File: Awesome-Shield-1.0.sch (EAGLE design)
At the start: 21 parts, among them J1 PORT1, J2 PORT2, J3 PORT3, SW1 SPST_TACT-EVQQ2, SW2 DPDT, U1 LIGHTSENSORTEMT6000, X1 PASSER-07, X2 PASSER-07

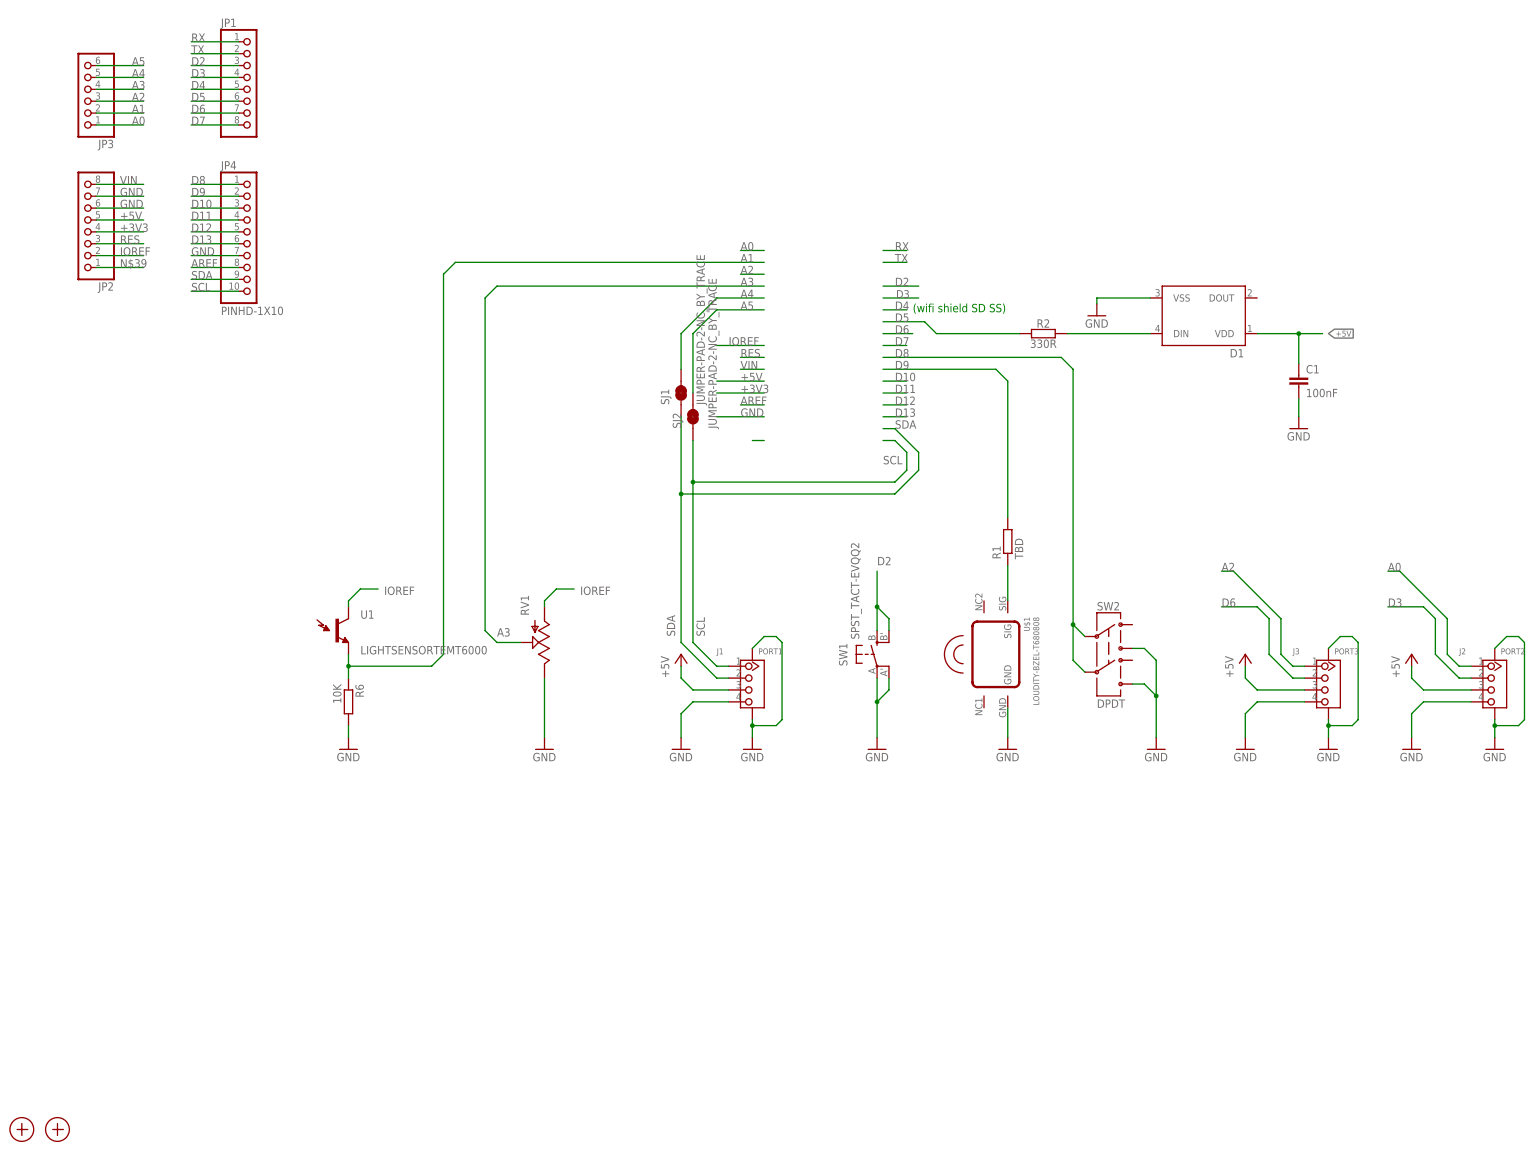
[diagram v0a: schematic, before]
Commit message: add resistors to button, toggleSwitch, knob signal lines
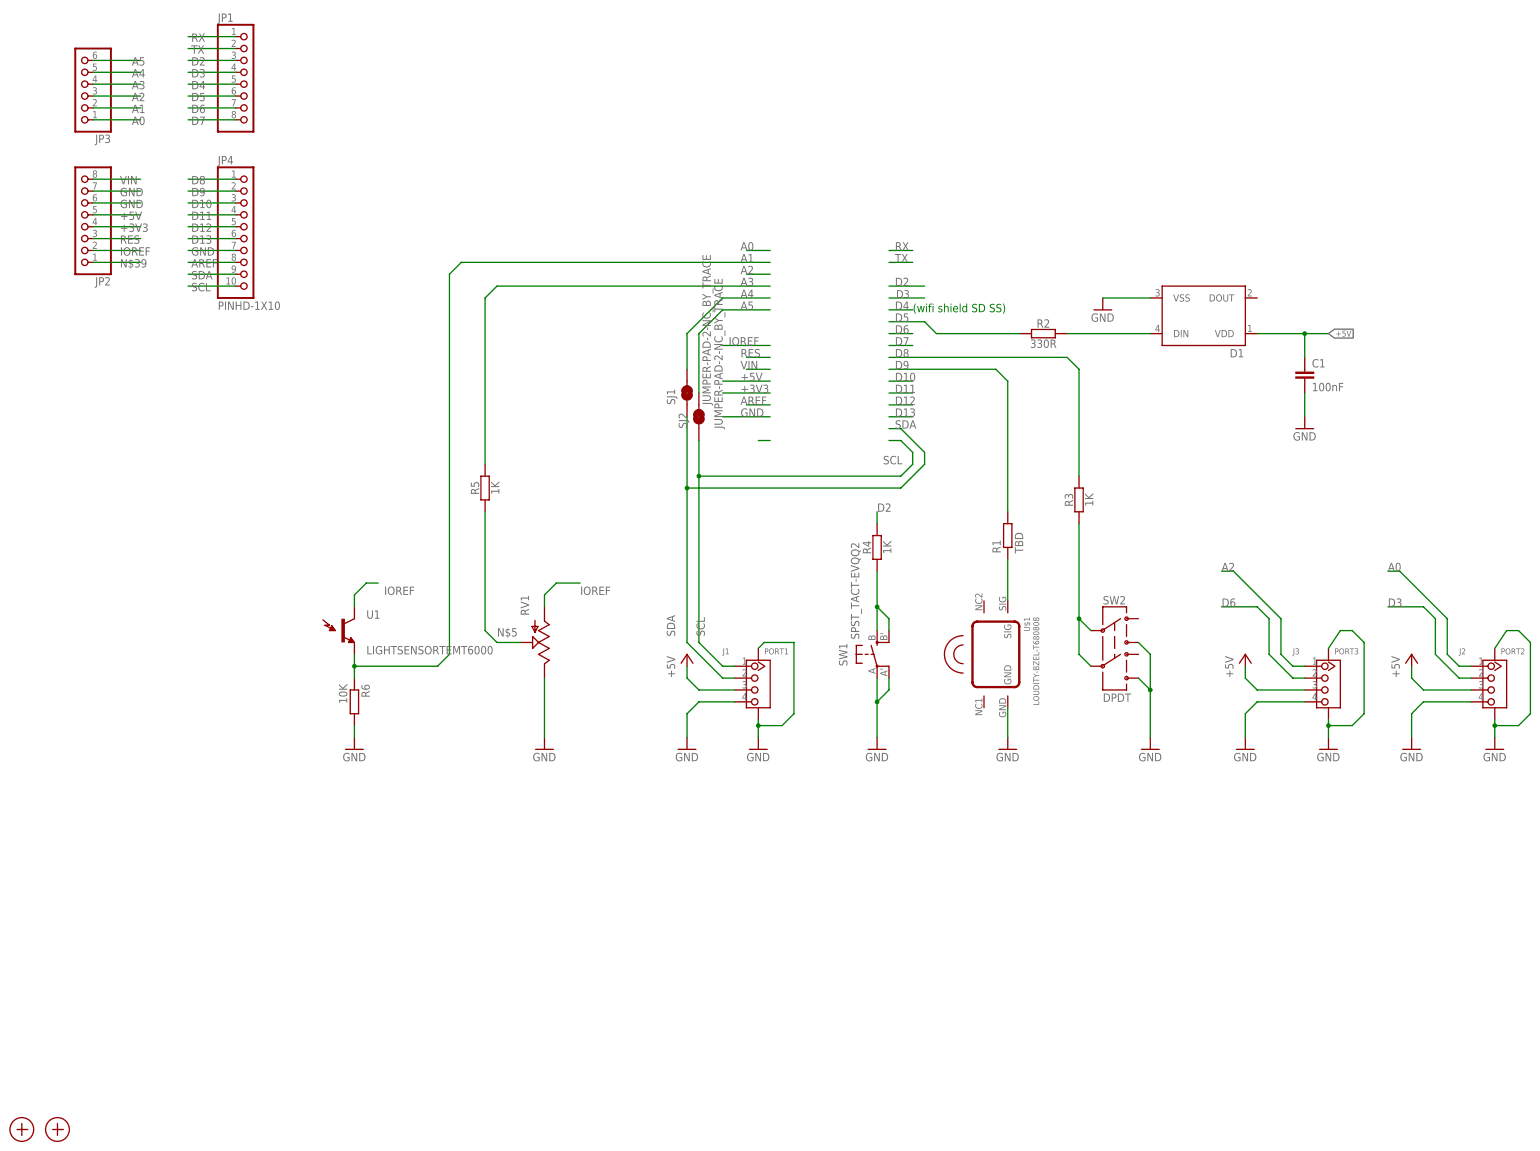
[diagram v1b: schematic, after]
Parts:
- added R3, R4, R5: 1K, we-rcl:RESISTOR-0603
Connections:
- new net N$4: R3.1, SW2.2, SW2.5
- new net N$5: R5.1, RV1.S
- new net N$6: R4.1, SW1.S, SW1.S1
- net A3: now also R5.2; no longer RV1.S
- net D2: now also R4.2; no longer SW1.S, SW1.S1
- net D8: now also R3.2; no longer SW2.2, SW2.5
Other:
- moved on the sheet: C1, J1, JP1, JP2, JP3, JP4, R1, R6, SJ1, SJ2, SW2, U1
